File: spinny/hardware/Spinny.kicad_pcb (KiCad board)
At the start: 2 copper layers, 60 x 60 mm, 36 parts, among them J1 USB_C_Receptacle_USB2.0, J2 Conn_01x04, SW1 SW_Push, SW2 SW_Push, SW3 SW_Push, SW4 SW_Push, SW5 SW_RST, U1 XC6206P332MR, U2 SRV05-4, U3 STM32F103C8T6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

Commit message: Spinny v2: fixes
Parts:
- turned SW2 to 0 degrees
- turned SW3 to 0 degrees
- turned SW4 to 0 degrees
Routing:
- net BTN_4: track 37.1 -> 39.1 mm
- net BTN_3: track 44.2 -> 46.2 mm
- net BTN_2: track 34.8 -> 36.8 mm
- net BTN_1: track 34.7 -> 36.7 mm

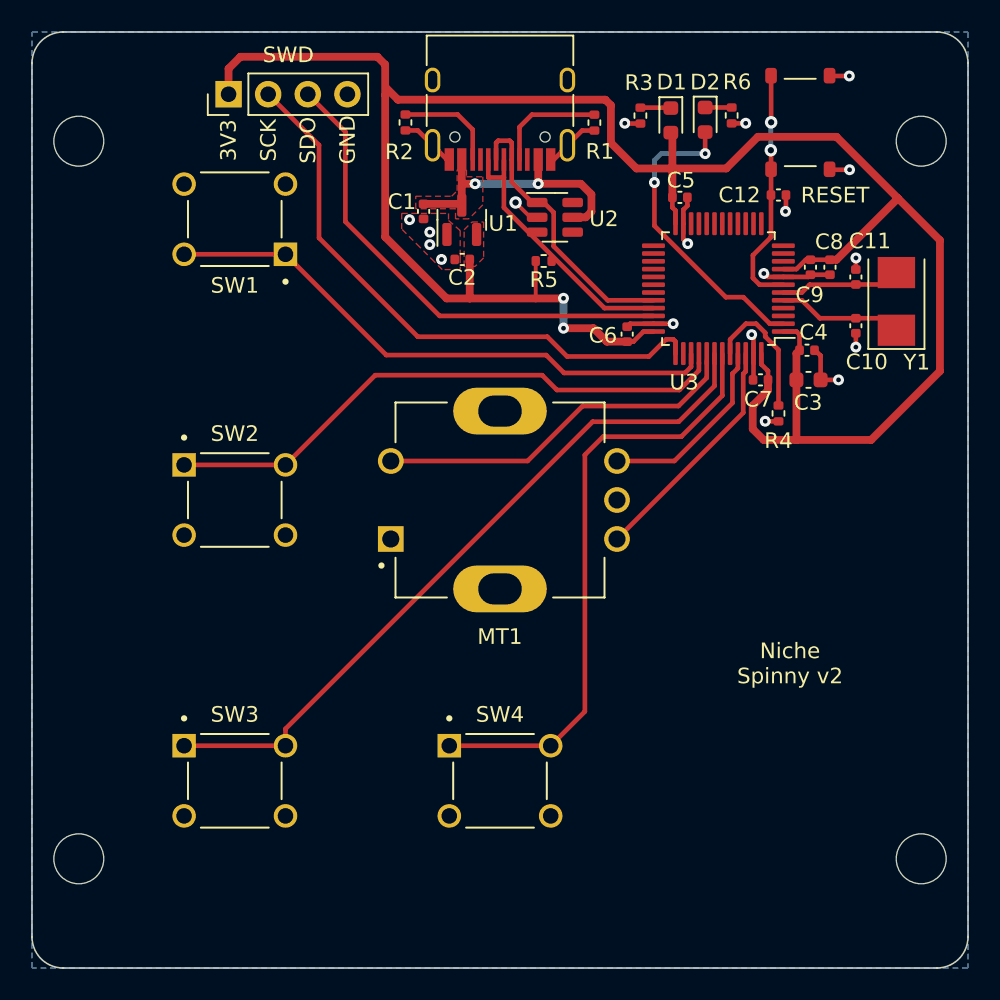
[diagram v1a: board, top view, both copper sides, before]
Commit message: Spinny V2 with stm32f104cbt6 instead of c8t6, because JLCPCB is random
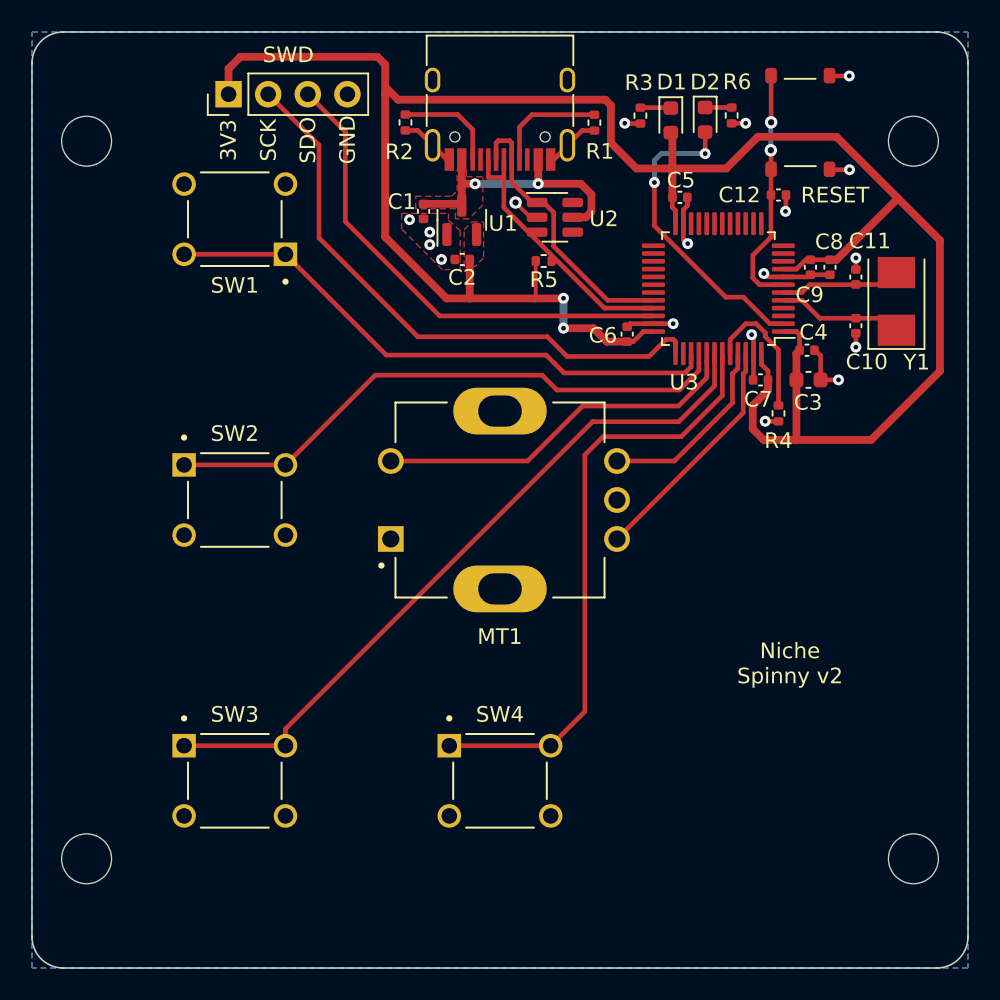
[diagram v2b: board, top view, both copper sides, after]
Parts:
- U3: value STM32F103C8T6 -> STM32F103CBT6
- moved H1 0.50 mm to (123.5, 77.0)
- moved H2 0.50 mm to (176.5, 77.0)
- moved H3 0.50 mm to (123.5, 123.0)
- moved H4 0.50 mm to (176.5, 123.0)
